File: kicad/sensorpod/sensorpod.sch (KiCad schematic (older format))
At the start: 79 parts

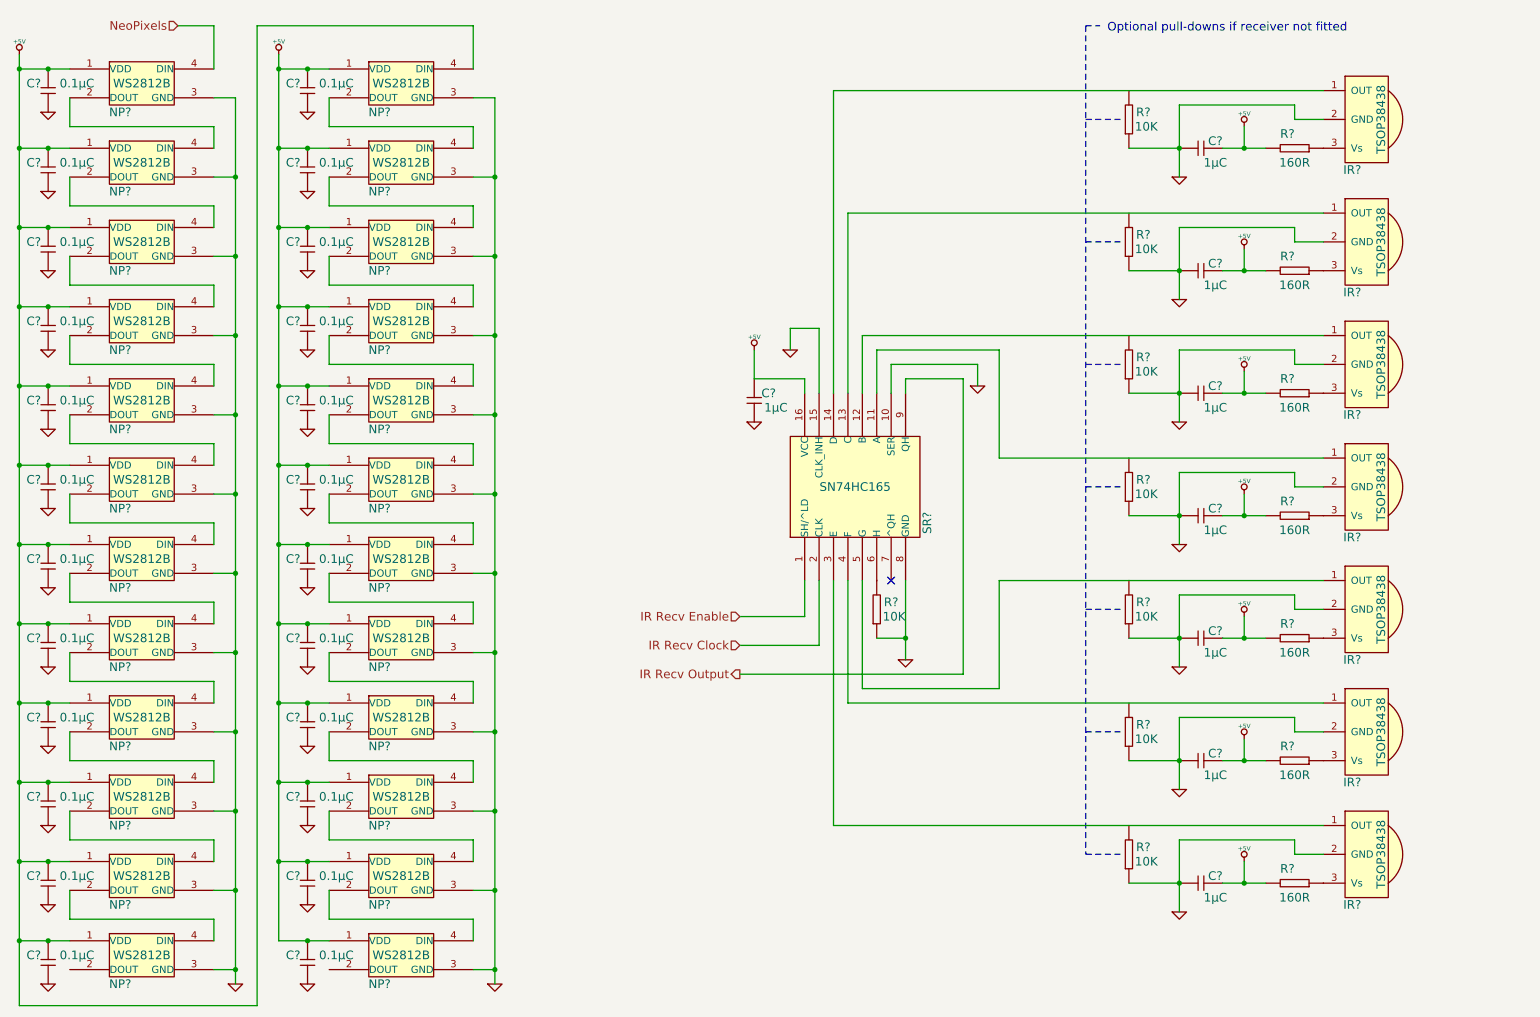
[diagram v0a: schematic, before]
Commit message: Started putting in footprints for sensorpod
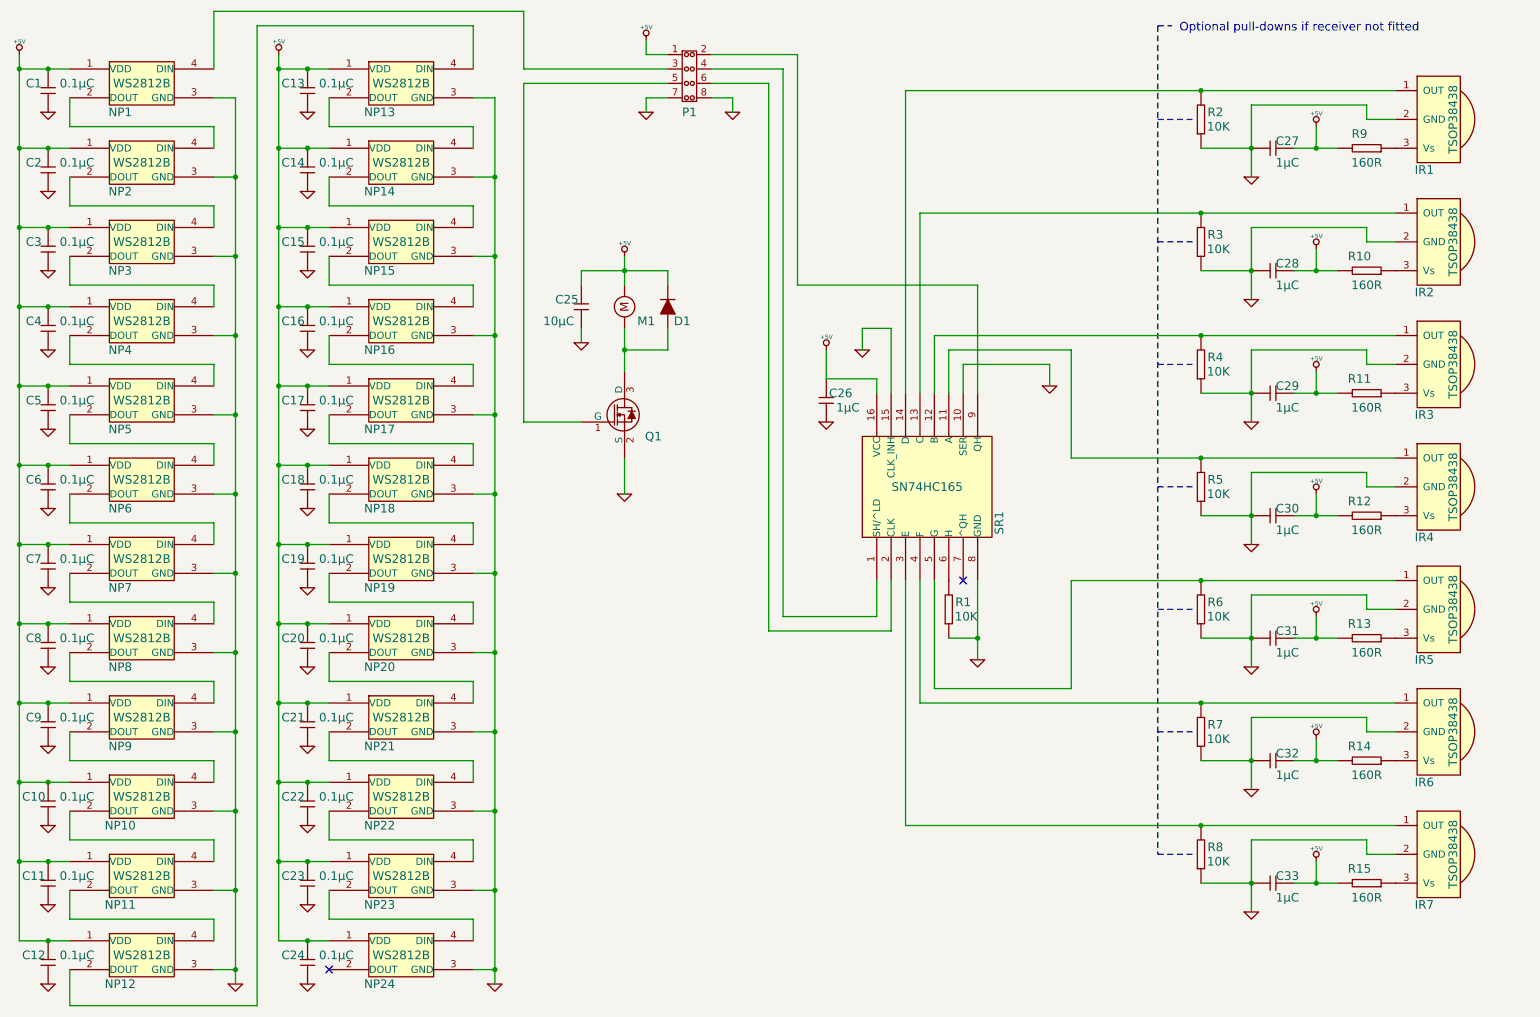
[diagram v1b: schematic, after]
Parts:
- added C25: GENERIC_CAPACITOR, ~, symbol GENERIC_CAPACITOR
- added D1: GENERIC_DIODE, symbol GENERIC_DIODE
- added M1: MOTOR, symbol MOTOR
- added P1: HEADER_(8_WAY), symbol HEADER_(8_WAY)
- added Q1: IRFML8244TRPBF, ~, symbol IRFML8244TRPBF
- gave numbers to parts that had none: 79
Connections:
- net +5V: now also C25.1, D1.2, M1.1, P1.1; no longer NP13.4 (DIN)
- net GND: now also C25.2, P1.7, P1.8, Q1.2 (S)
- net at NP12.2 (DOUT): now also NP13.4 (DIN)
- net at IR4.1 (OUT), SR1.11 (A): now also R5.1
- net at IR3.1 (OUT), SR1.12 (B): now also R4.1
- net at IR2.1 (OUT), SR1.13 (C): now also R3.1
- net at IR1.1 (OUT), SR1.14 (D): now also R2.1
- net at IR7.1 (OUT), SR1.3 (E): now also R8.1
- net at IR6.1 (OUT), SR1.4 (F): now also R7.1
- net at IR5.1 (OUT), SR1.5 (G): now also R6.1
- net IR Recv Clock: no longer names the net of SR1.2 (CLK)
- net IR Recv Clock: now also P1.6
- net IR Recv Enable: no longer names the net of SR1.1 (SH/^LD)
- net IR Recv Enable: now also P1.4
- net IR Recv Output: no longer names the net of SR1.9 (QH)
- net IR Recv Output: now also P1.2
- net NeoPixels: no longer names the net of NP1.4 (DIN)
- net NeoPixels: now also P1.3
- new net: P1.5, Q1.1 (G)
- new net: D1.1, M1.2, Q1.3 (D)
- no-connect marks 1 -> 2
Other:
- moved on the sheet: C26, C27, C28, C29, C30, C31, C32, C33, IR1, IR2, IR3, IR4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

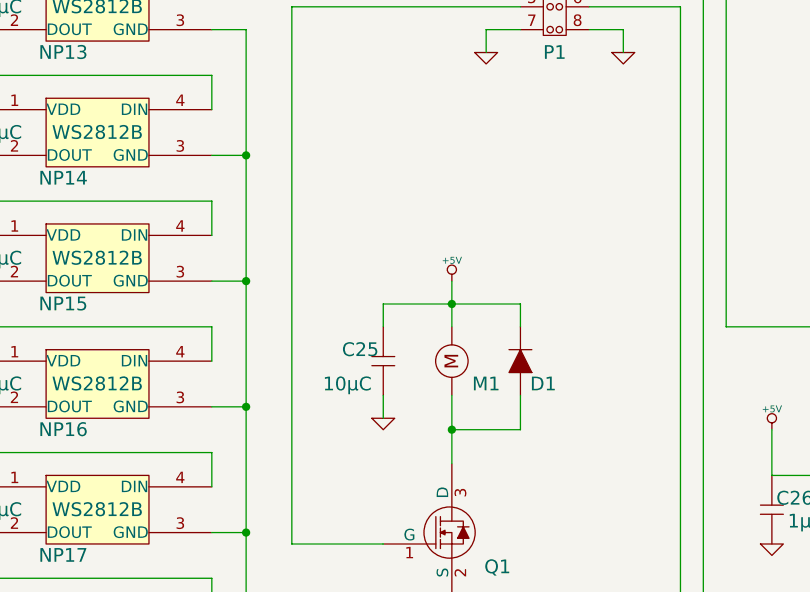
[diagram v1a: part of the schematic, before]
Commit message: Sensor pod footprints all in
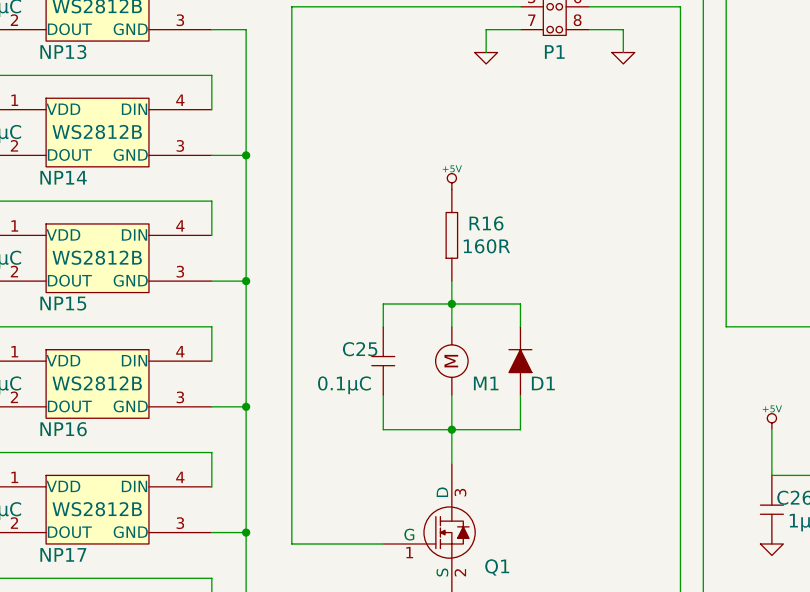
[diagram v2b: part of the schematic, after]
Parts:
- added R16: GENERIC_RESISTOR, 0805, symbol GENERIC_RESISTOR
- C1, C10, C11, C12, C13, C14, C15, C16, C17, C18, C19, C2, C20, C21, C22, C23, C24, C26, C27, C28, C29, C3, C30, C31, C32, C33, C4, C5, C6, C7, C8, C9, R1, R10, R11, R12, R13, R14, R15, R2, R3, R4, R5, R6, R7, R8, R9: footprint ~ -> 0805
- C25: footprint ~ -> 0805; Capacitance 10µC -> 0.1µC
- D1: footprint (none) -> SOD-323
- IR1, IR2, IR3, IR4, IR5, IR6, IR7: footprint ~ -> Minicast
- M1: footprint (none) -> Header_2x1
- NP1, NP10, NP11, NP12, NP13, NP14, NP15, NP16, NP17, NP18, NP19, NP2, NP20, NP21, NP22, NP23, NP24, NP3, NP4, NP5, NP6, NP7, NP8, NP9: footprint ~ -> 5050
- P1: footprint (none) -> Header_4x2
- Q1: footprint ~ -> SOT-23
- SR1: footprint ~ -> SOIC-16
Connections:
- net +5V: now also R16.1; no longer C25.1, D1.2, M1.1
- net GND: no longer C25.2
- net at D1.1, M1.2, Q1.3 (D): now also C25.2
- new net: C25.1, D1.2, M1.1, R16.2

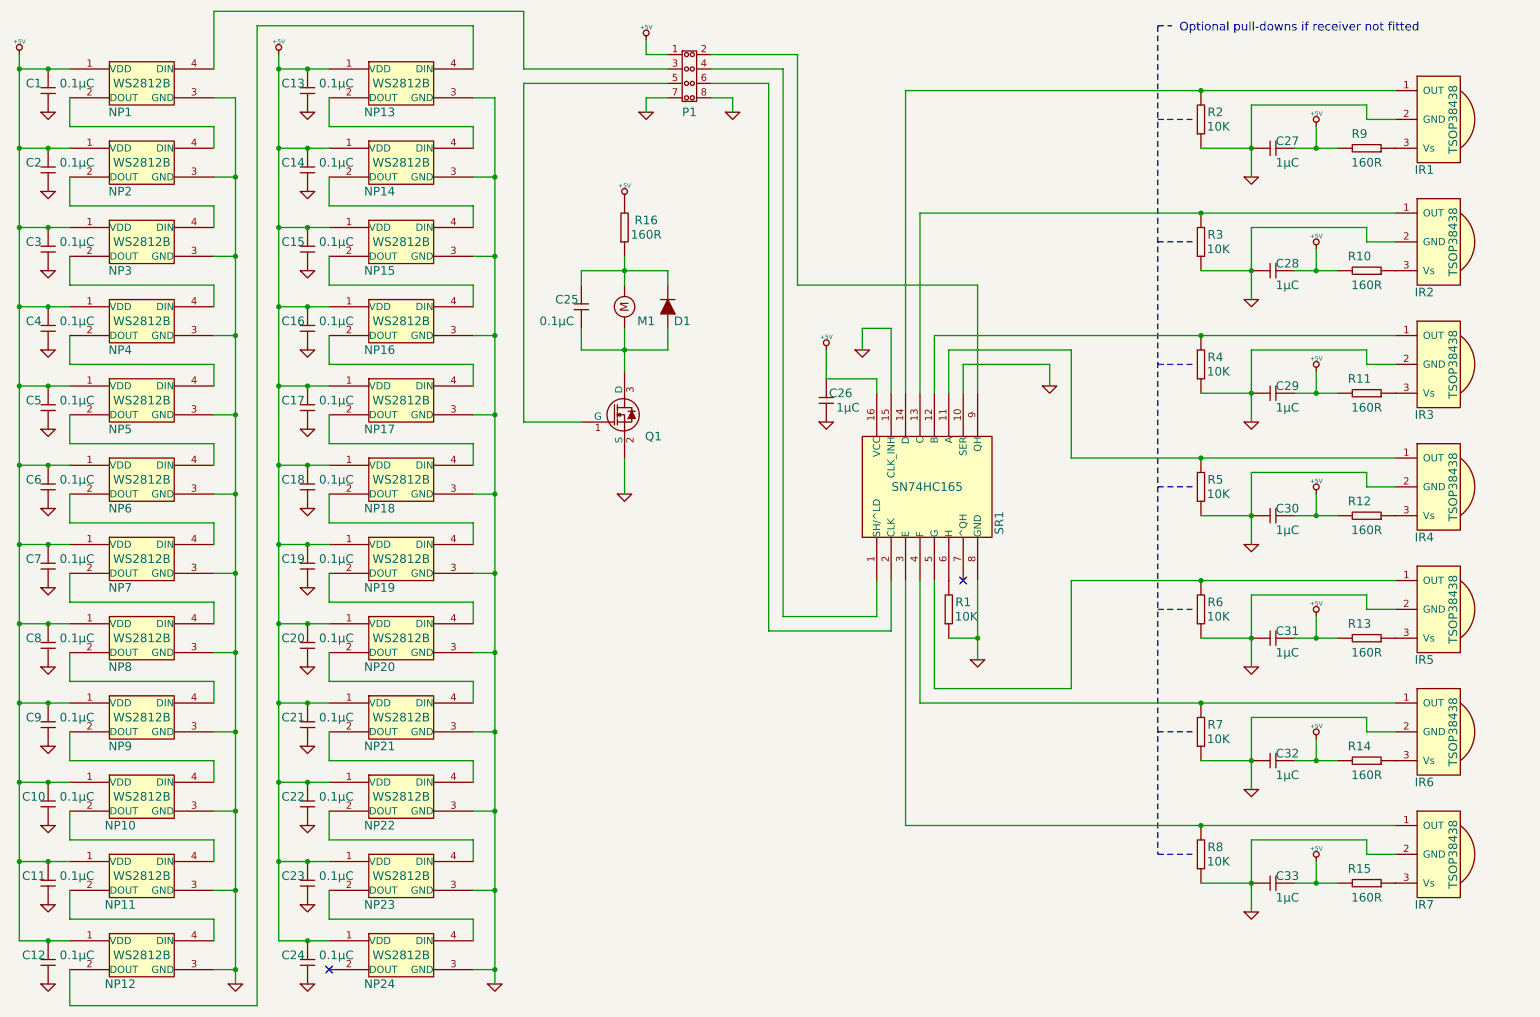
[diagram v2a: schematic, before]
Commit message: Reduced component count so it will fit
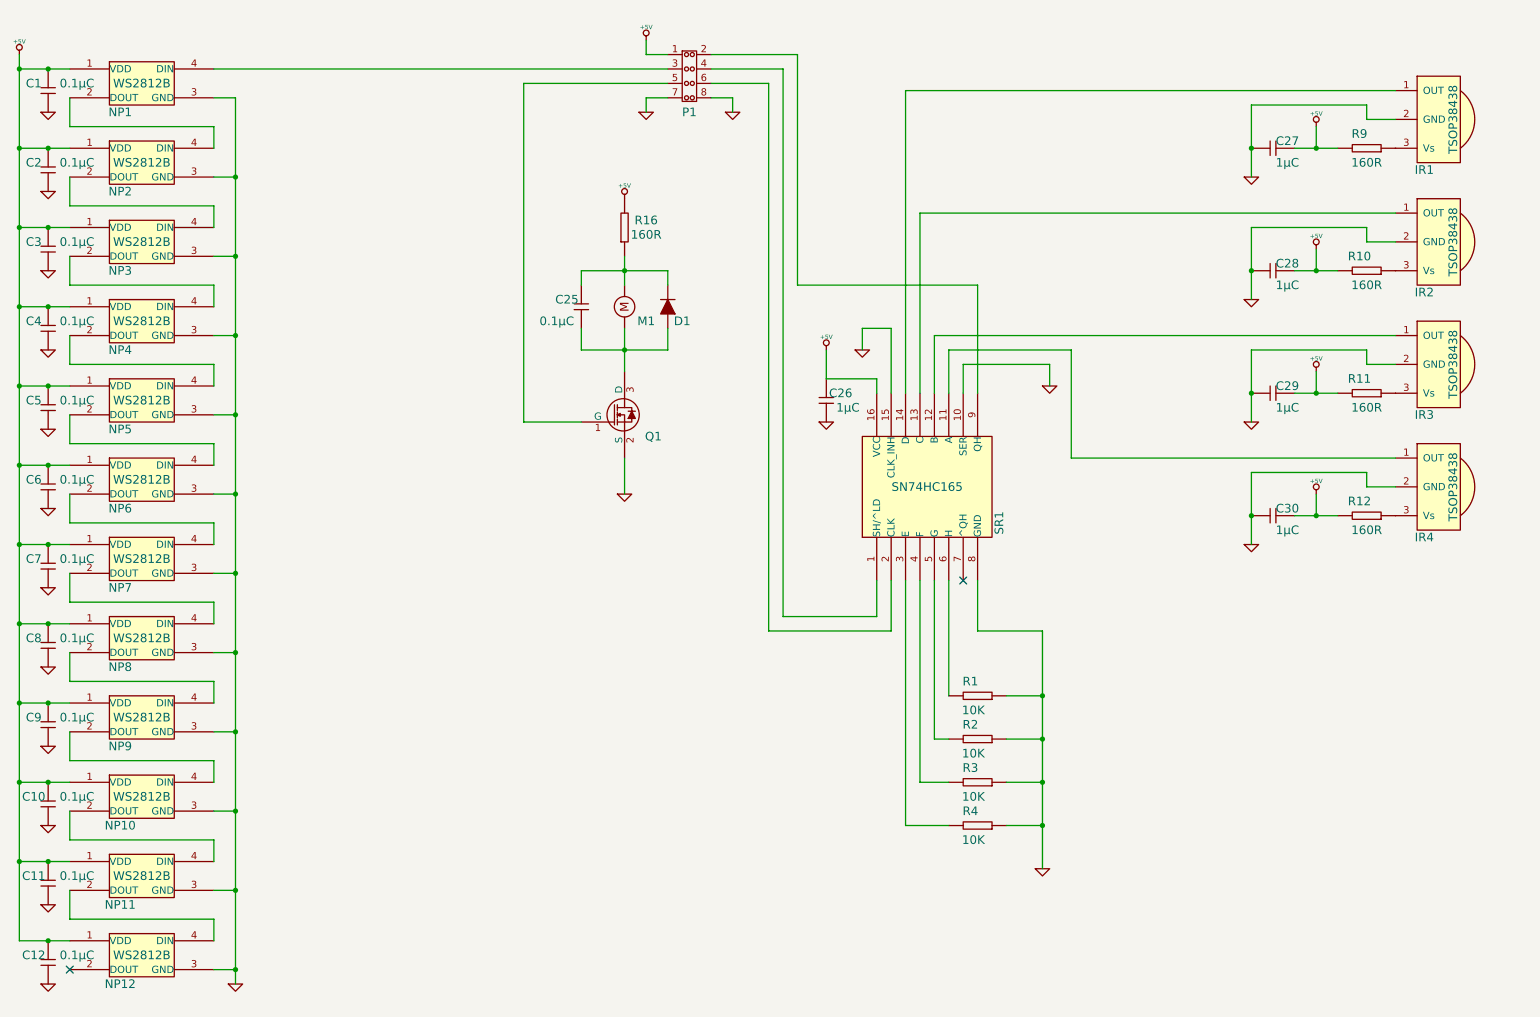
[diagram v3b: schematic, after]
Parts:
- removed C13, C14, C15, C16, C17, C18, C19, C20, C21, C22, C23, C24, C31, C32, C33: GENERIC_CAPACITOR, 0805, symbol GENERIC_CAPACITOR
- removed IR5, IR6, IR7: TSOP38438, Minicast, symbol TSOP38438
- removed NP13, NP14, NP15, NP16, NP17, NP18, NP19, NP20, NP21, NP22, NP23, NP24: WS2812B, 5050, symbol WS2812B
- removed R13, R14, R15, R5, R6, R7, R8: GENERIC_RESISTOR, 0805, symbol GENERIC_RESISTOR
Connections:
- net at IR3.1 (OUT), SR1.12 (B): no longer R4.1
- net at IR2.1 (OUT), SR1.13 (C): no longer R3.1
- net at IR1.1 (OUT), SR1.14 (D): no longer R2.1
- net at SR1.3 (E): now also R4.1
- net at SR1.4 (F): now also R3.1
- net at SR1.5 (G): now also R2.1
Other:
- note removed: "Optional pull-downs if receiver not fitted"
- moved on the sheet: R1, R2, R3, R4
